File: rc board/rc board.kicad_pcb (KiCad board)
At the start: 2 copper layers, 96.3 x 68.9 mm, 95 parts, among them J1 Bypass, J10 3S, J11 4S, J12 5S, J13 6S, J14 Mot_0, J15 Mot_1, J16 Mot_3, J17 Mot_2, J2 Bypass, J3 Bypass, J4 Throttle_in, J5 Throttle_out, J6 CH3_in, J7 CH3_out, J8 Steering_in, J9 Steering_out, U1 DRV10983, U2 DRV10983, U3 DRV10983, U4 DRV10983

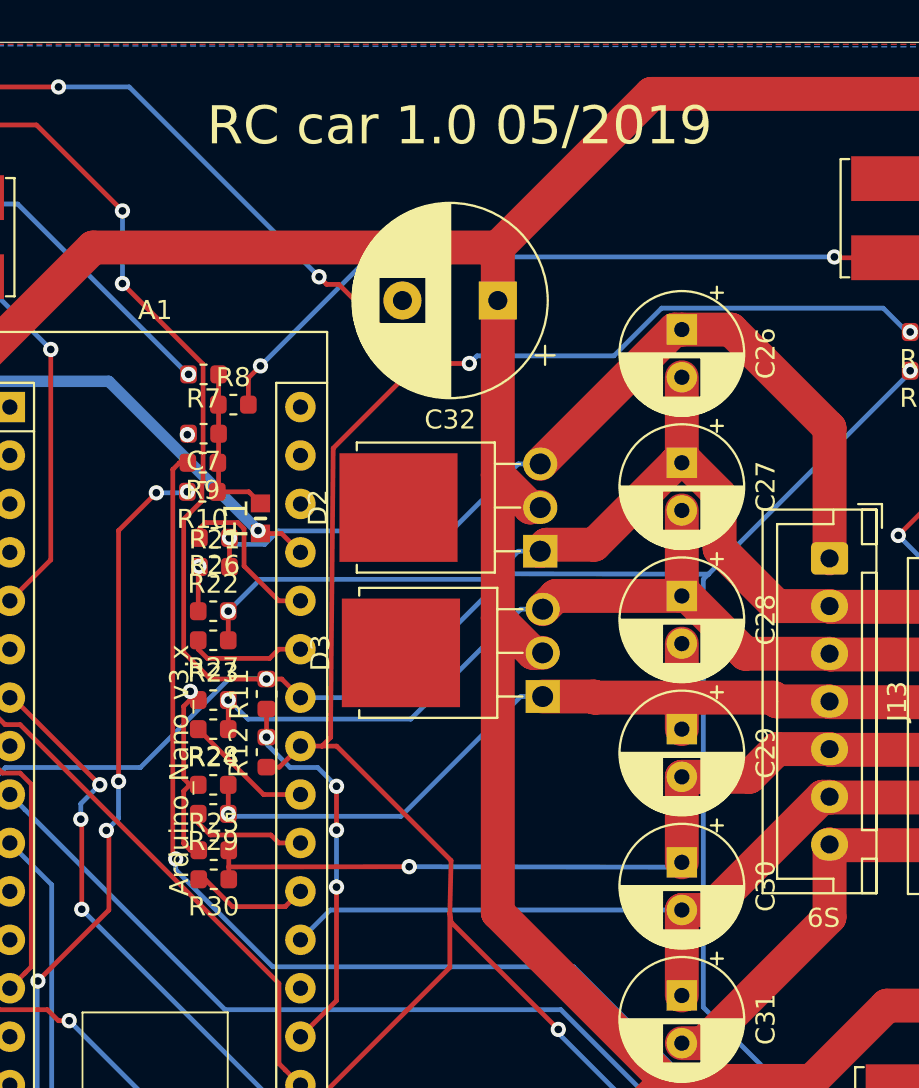
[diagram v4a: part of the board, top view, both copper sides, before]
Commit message: Added bleed resistors in parallel to the caps to allow for a single big cell (bench PSU) to be used.
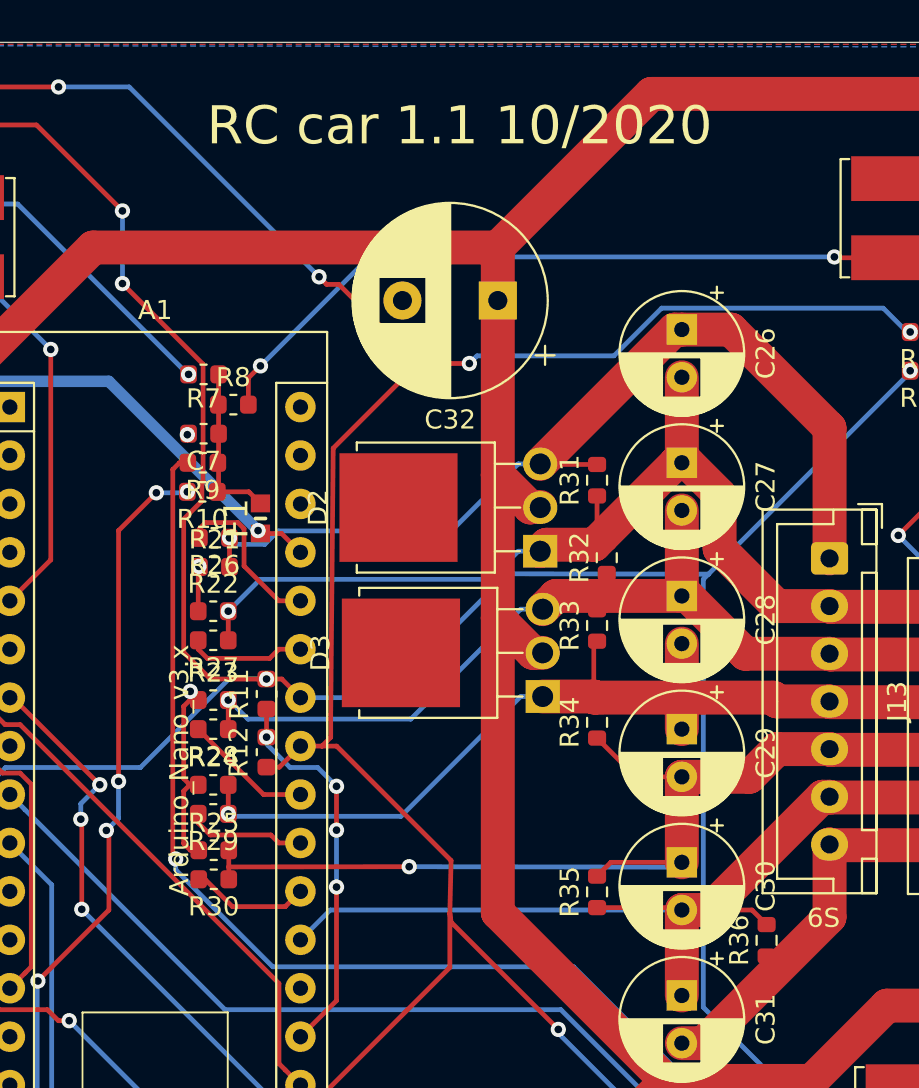
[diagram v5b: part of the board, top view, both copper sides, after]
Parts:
- added R31: 10k, Resistor_SMD:R_0603_1608Metric, F.Cu at (71.1, 38.1)
- added R32: 10k, Resistor_SMD:R_0603_1608Metric, F.Cu at (71.6, 42.2)
- added R33: 10k, Resistor_SMD:R_0603_1608Metric, F.Cu at (71.1, 45.7)
- added R34: 10k, Resistor_SMD:R_0603_1608Metric, F.Cu at (71.1, 50.8)
- added R35: 10k, Resistor_SMD:R_0603_1608Metric, F.Cu at (71.1, 59.7)
- added R36: 10k, Resistor_SMD:R_0603_1608Metric, F.Cu at (80.0, 62.2)
- C26, C27, C28, C29, C30, C31: value 1000uF -> 470uF
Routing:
- net Batt_1: track 61.1 -> 71.2 mm
- net Batt_0: track 58.3 -> 67.5 mm
- net Batt_5: track 46.9 -> 49.9 mm
- net Batt_2: track 63.2 -> 66.2 mm
- net Batt_4: track 53.3 -> 56.0 mm
- net Batt_3: track 57.2 -> 58.4 mm
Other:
- board text added: "RC car 1.1 10/2020"
- board text removed: "RC car 1.0 05/2019"
